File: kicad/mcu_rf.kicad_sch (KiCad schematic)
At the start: 5 parts, among them J1 Conn_Coaxial

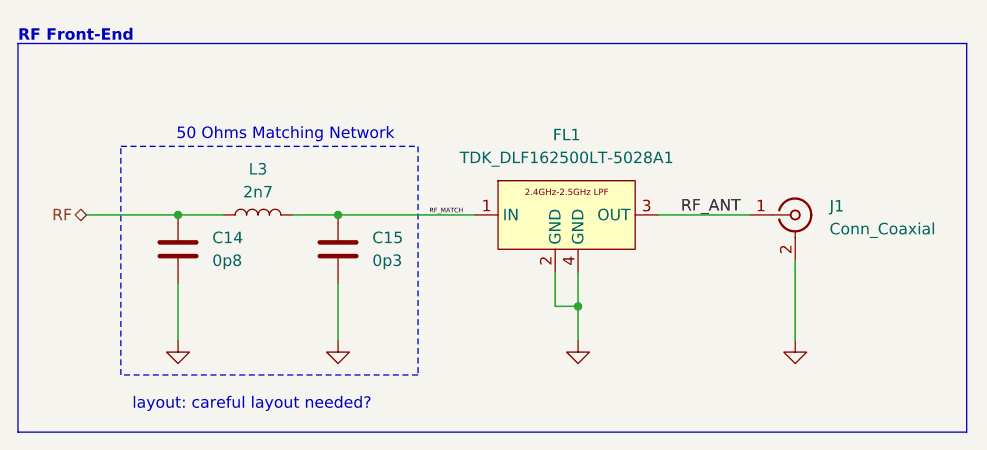
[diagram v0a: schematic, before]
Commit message: refactor(schematic): polish the schematic as much as possible - add new Basmala - fix netlist names almost EVERYWHERE, this is to help with net classes, and to help with building a good habit of naming nets properly - add a 100n capacitor to the SWD connector power pin - update many many other things EVERYWHERE
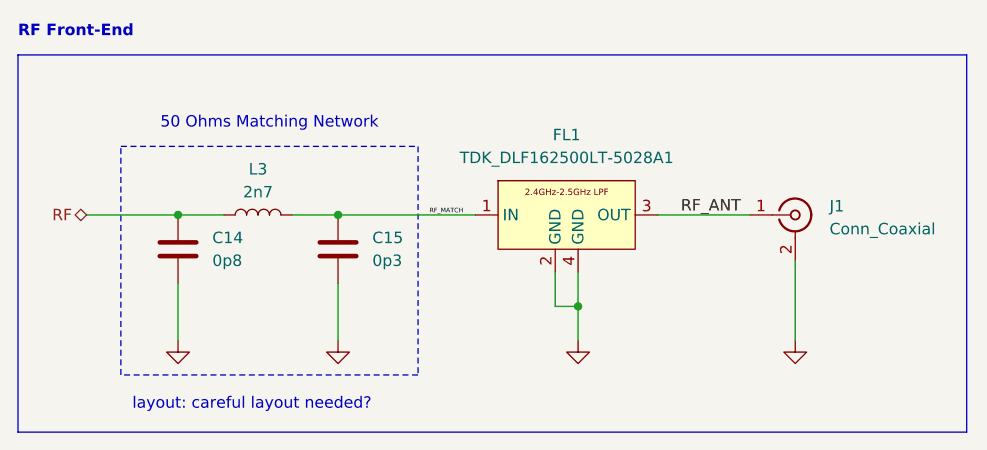
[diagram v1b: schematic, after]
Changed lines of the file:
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@@
 	)
 	(rectangle
-		(start 88.9 74.93)
+		(start 88.9 76.2)
 		(end 194.31 118.11)
 		(stroke
@@
 	(text "50 Ohms Matching Network"
 		(exclude_from_sim no)
-		(at 118.618 85.09 0)
+		(at 116.84 83.82 0)
 		(effects
 			(font
@@
 	(text "RF Front-End"
 		(exclude_from_sim no)
-		(at 88.9 74.168 0)
+		(at 88.9 73.66 0)
 		(effects
 			(font
